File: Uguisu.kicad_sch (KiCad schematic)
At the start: 8 parts, among them U1 XIAO-nRF52840-SMD

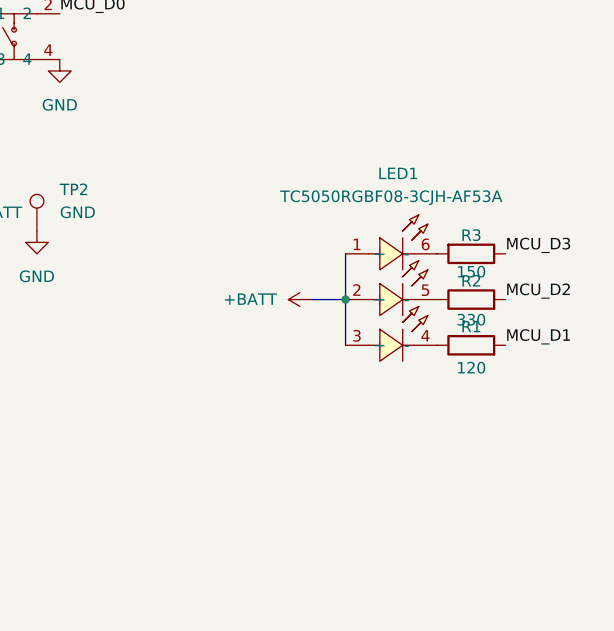
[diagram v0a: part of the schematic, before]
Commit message: LED pin order and docs: D1=Blue, D2=Red, D3=Green; R1=Blue, R2=Red, R3=Green; LED1 pins 1/2/3
Made-with: Cursor
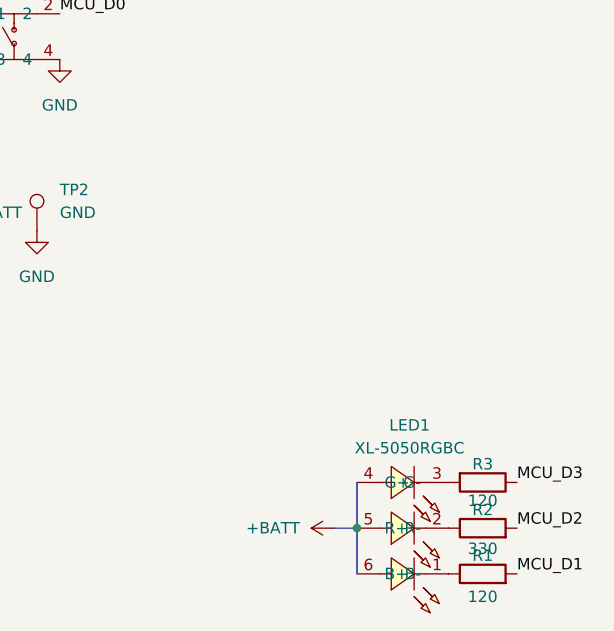
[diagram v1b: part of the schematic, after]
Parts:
- removed LED1: TC5050RGBF08-3CJH-AF53A, easyeda2kicad:LED-SMD_6P-L5.0-W5.0-TL_TC5050RGBF08, symbol easyeda2kicad:TC5050RGBF08-3CJH-AF53A
- added LED1: XL-5050RGBC, easyeda2kicad:LED-ARRAY-SMD_6P-L5.0-W5.0-TL-RD_3, symbol easyeda2kicad:XL-5050RGBC
- R3: value 150 -> 120
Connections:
- net at R1.1: now also LED1.1 (B-)
- net at R2.1: now also LED1.2 (R-)
- net at R3.2: now also LED1.3 (G-)
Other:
- moved on the sheet: R1, R2, R3
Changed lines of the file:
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@@
 	(paper "A4")
 	(junction
-		(at 144.78 91.44)
+		(at 146.05 116.84)
 		(diameter 0)
 		(color 0 0 0 0)
@@
 	(bus
 		(pts
-			(xy 144.78 91.44) (xy 144.78 96.52)
+			(xy 143.51 116.84) (xy 146.05 116.84)
 		)
 		(stroke
@@
 	(bus
 		(pts
-			(xy 140.97 91.44) (xy 144.78 91.44)
+			(xy 146.05 116.84) (xy 146.05 121.92)
 		)
 		(stroke
@@
 	(bus
 		(pts
-			(xy 144.78 86.36) (xy 144.78 91.44)
+			(xy 146.05 111.76) (xy 146.05 116.84)
 		)
 		(stroke
@@
 	)
 	(label "MCU_D2"
-		(at 162.56 91.44 0)
+		(at 163.83 116.84 0)
 		(effects
 			(font
@@
 	)
 	(label "MCU_D3"
-		(at 162.56 86.36 0)
+		(at 163.83 111.76 0)
 		(effects
 			(font
@@
 	)
 	(label "MCU_D1"
-		(at 162.56 96.52 0)
+		(at 163.83 121.92 0)
 		(effects
 			(font
@@
 	(symbol
 		(lib_id "power:+BATT")
-		(at 140.97 91.44 90)
+		(at 143.51 116.84 90)
 		(unit 1)
 		(exclude_from_sim no)
@@
 		(fields_autoplaced yes)
 		(property "Reference" "#PWR010"
-			(at 144.78 91.44 0)
+			(at 147.32 116.84 0)
 			(effects
 				(font
@@
 		)
 		(property "Value" "+BATT"
-			(at 137.16 91.4399 90)
+			(at 139.7 116.8399 90)
 			(effects
 				(font
@@
 		)
 		(property "Footprint" ""
-			(at 140.97 91.44 0)
+			(at 143.51 116.84 0)
 			(effects
 				(font
@@
 		)
 		(property "Datasheet" ""
-			(at 140.97 91.44 0)
+			(at 143.51 116.84 0)
 			(effects
 				(font
@@
 		)
 		(property "Description" "Power symbol creates a global label with name \"+BATT\""
-			(at 140.97 91.44 0)
+			(at 143.51 116.84 0)
 			(effects
 				(font
@@
 	)
 	(symbol
-		(lib_id "easyeda2kicad:TC5050RGBF08-3CJH-AF53A")
-		(at 149.86 91.44 0)
-		(unit 1)
-		(exclude_from_sim no)
-		(in_bom yes)
-		(on_board yes)
-		(dnp no)
+		(lib_id "easyeda2kicad:XL-5050RGBC")
+		(at 151.13 121.92 180)
+		(unit 1)
+		(exclude_from_sim no)
+		(in_bom yes)
+		(on_board yes)
+		(dnp no)
+		(fields_autoplaced yes)
 		(property "Reference" "LED1"
-			(at 150.62 77.47 0)
-			(effects
-				(font
-					(size 1.27 1.27)
-				)
-			)
-		)
-		(property "Value" "TC5050RGBF08-3CJH-AF53A"
-			(at 149.86 80.01 0)
-			(effects
-				(font
-					(size 1.27 1.27)
-				)
-			)
-		)
-		(property "Footprint" "easyeda2kicad:LED-SMD_6P-L5.0-W5.0-TL_TC5050RGBF08"
-			(at 149.86 104.14 0)
-			(effects
-				(font
-					(size 1.27 1.27)
-				)
-				(hide yes)
-			)
-		)
-		(property "Datasheet" "https://lcsc.com/product-detail/Light-Emitting-Diodes-LED_TCWIN-TC5050RGBF08-3CJH-AF53A_C784540.html"
-			(at 149.86 106.68 0)
+			(at 151.89 105.41 0)
+			(effects
+				(font
+					(size 1.27 1.27)
+				)
+			)
+		)
+		(property "Value" "XL-5050RGBC"
+			(at 151.89 107.95 0)
+			(effects
+				(font
+					(size 1.27 1.27)
+				)
+			)
+		)
+		(property "Footprint" "easyeda2kicad:LED-ARRAY-SMD_6P-L5.0-W5.0-TL-RD_3"
+			(at 151.13 104.14 0)
+			(effects
+				(font
+					(size 1.27 1.27)
+				)
+				(hide yes)
+			)
+		)
+		(property "Datasheet" ""
+			(at 151.13 121.92 0)
 			(effects
 				(font
@@
 		)
 		(property "Description" ""
-			(at 149.86 91.44 0)
-			(effects
-				(font
-					(size 1.27 1.27)
-				)
-				(hide yes)
-			)
-		)
-		(property "LCSC Part" "C784540"
-			(at 149.86 109.22 0)
+			(at 151.13 121.92 0)
+			(effects
+				(font
+					(size 1.27 1.27)
+				)
+				(hide yes)
+			)
+		)
+		(property "LCSC Part" "C2843868"
+			(at 151.13 101.6 0)
 			(effects
 				(font
@@
 		(pin "2"
 		)
+		(pin "3"
+		)
+		(pin "1"
+		)
 		(pin "5"
 		)
-		(pin "1"
+		(pin "4"
 		)
 		(pin "6"
 		)
-		(pin "4"
-		)
-		(pin "3"
-		)
 		(instances
 			(project ""
@@
 	(symbol
 		(lib_id "Device:R")
-		(at 158.75 96.52 90)
+		(at 160.02 121.92 90)
 		(unit 1)
 		(exclude_from_sim no)
@@
 		(dnp no)
 		(property "Reference" "R1"
-			(at 158.75 94.488 90)
+			(at 160.02 119.888 90)
 			(effects
 				(font
@@
 		)
 		(property "Value" "120"
-			(at 158.75 99.06 90)
+			(at 160.02 124.46 90)
 			(effects
 				(font
@@
 		)
 		(property "Footprint" "Resistor_SMD:R_0603_1608Metric"
-			(at 158.75 98.298 90)
+			(at 160.02 123.698 90)
 			(effects
 				(font
@@
 		)
 		(property "Datasheet" "~"
-			(at 158.75 96.52 0)
+			(at 160.02 121.92 0)
 			(effects
 				(font
@@
 		)
 		(property "Description" "Resistor"
-			(at 158.75 96.52 0)
+			(at 160.02 121.92 0)
 			(effects
 				(font
@@
 	(symbol
 		(lib_id "Device:R")
-		(at 158.75 91.44 90)
+		(at 160.02 116.84 90)
 		(unit 1)
 		(exclude_from_sim no)
@@
 		(dnp no)
 		(property "Reference" "R2"
-			(at 158.75 89.408 90)
+			(at 160.02 114.808 90)
 			(effects
 				(font
@@
 		)
 		(property "Value" "330"
-			(at 158.75 93.726 90)
+			(at 160.02 119.126 90)
 			(effects
 				(font
@@
 		)
 		(property "Footprint" "Resistor_SMD:R_0603_1608Metric"
-			(at 158.75 93.218 90)
+			(at 160.02 118.618 90)
 			(effects
 				(font
@@
 		)
 		(property "Datasheet" "~"
-			(at 158.75 91.44 0)
+			(at 160.02 116.84 0)
 			(effects
 				(font
@@
 		)
 		(property "Description" "Resistor"
-			(at 158.75 91.44 0)
+			(at 160.02 116.84 0)
 			(effects
 				(font
@@
 	(symbol
 		(lib_id "Device:R")
-		(at 158.75 86.36 270)
+		(at 160.02 111.76 270)
 		(unit 1)
 		(exclude_from_sim no)
@@
 		(dnp no)
 		(property "Reference" "R3"
-			(at 158.75 84.328 90)
-			(effects
-				(font
-					(size 1.27 1.27)
-				)
-			)
-		)
-		(property "Value" "150"
-			(at 158.75 88.392 90)
+			(at 160.02 109.728 90)
+			(effects
+				(font
+					(size 1.27 1.27)
+				)
+			)
+		)
+		(property "Value" "120"
+			(at 160.02 113.792 90)
 			(effects
 				(font
@@
 		)
 		(property "Footprint" "Resistor_SMD:R_0603_1608Metric"
-			(at 158.75 84.582 90)
+			(at 160.02 109.982 90)
 			(effects
 				(font
@@
 		)
 		(property "Datasheet" "~"
-			(at 158.75 86.36 0)
+			(at 160.02 111.76 0)
 			(effects
 				(font
@@
 		)
 		(property "Description" "Resistor"
-			(at 158.75 86.36 0)
-			(effects
-				(font
+			(at 160.02 111.76 0)
+			(effects
+				(font
